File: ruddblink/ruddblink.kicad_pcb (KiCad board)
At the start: 2 copper layers, 40.6 x 48.5 mm, 30 parts, among them Q1 IRFML8244, SW1 JS202011JCQN, SW2 PTS526 SK15 SMTR2 LFS, U1 ATtiny85-20SU, U2 74HC595

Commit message: Add OSHW symbol
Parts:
- added G***: LOGO, ruddblink:OSHW-Symbol_140mil, B.Cu at (128.3, 104.1)

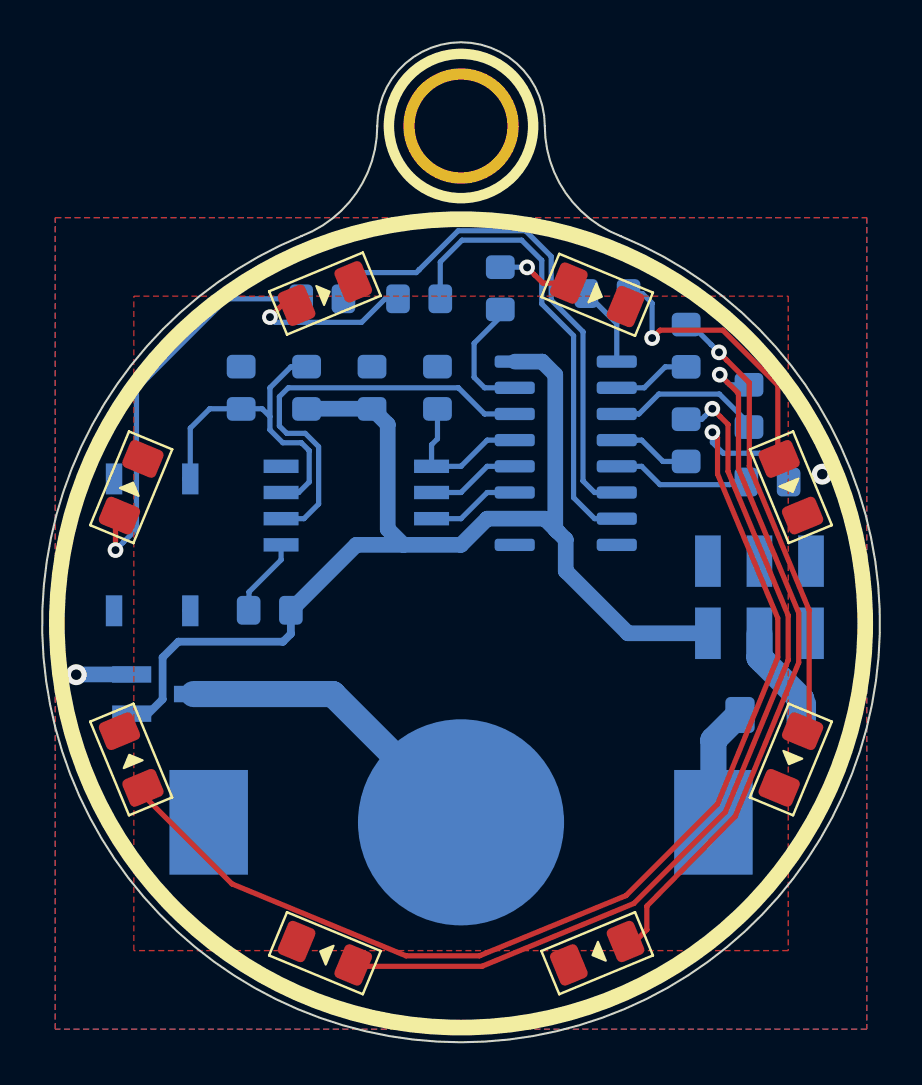
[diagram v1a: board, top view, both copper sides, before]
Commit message: Additional cosmetic edits
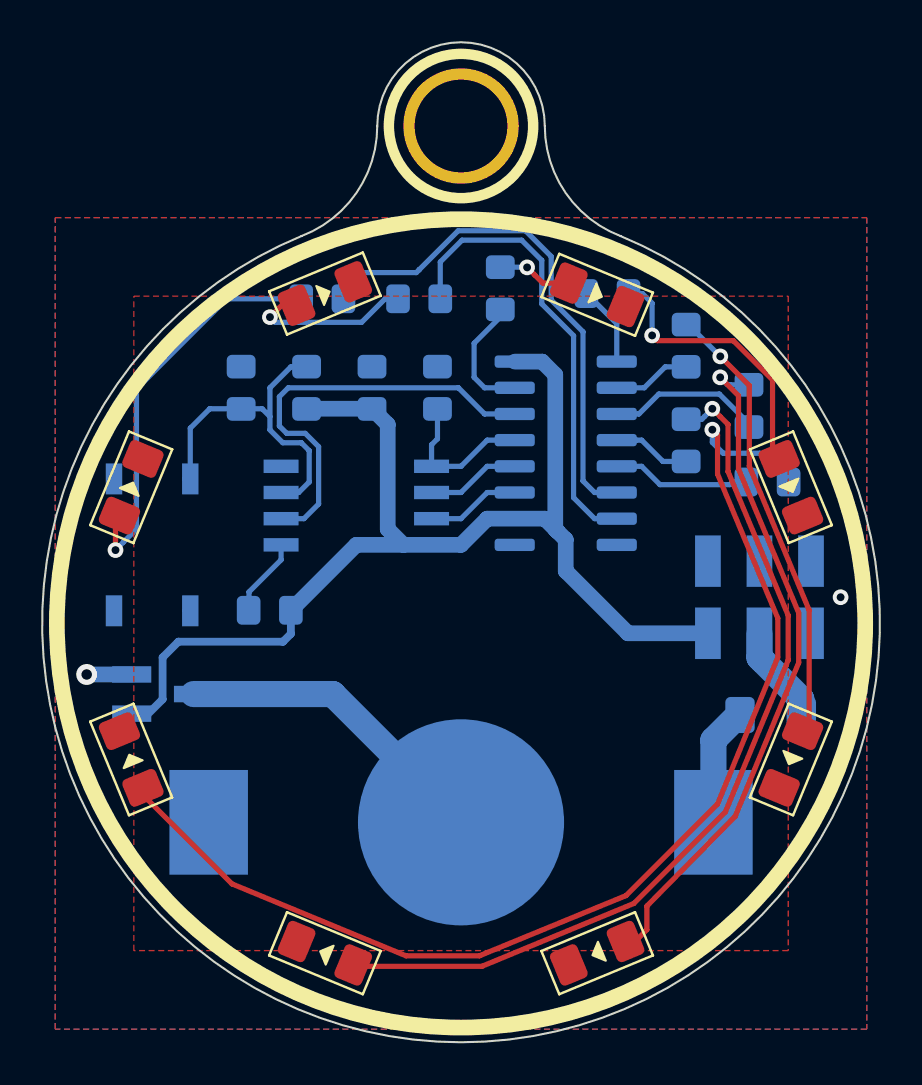
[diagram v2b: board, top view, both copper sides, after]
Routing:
- net GND: track 2.70 -> 2.18 mm
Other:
- board text added: "-"

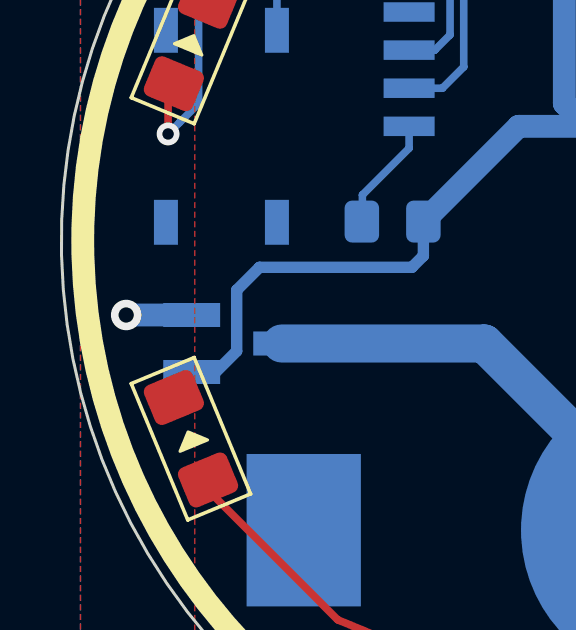
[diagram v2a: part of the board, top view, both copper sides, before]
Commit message: Fix some DFM issues
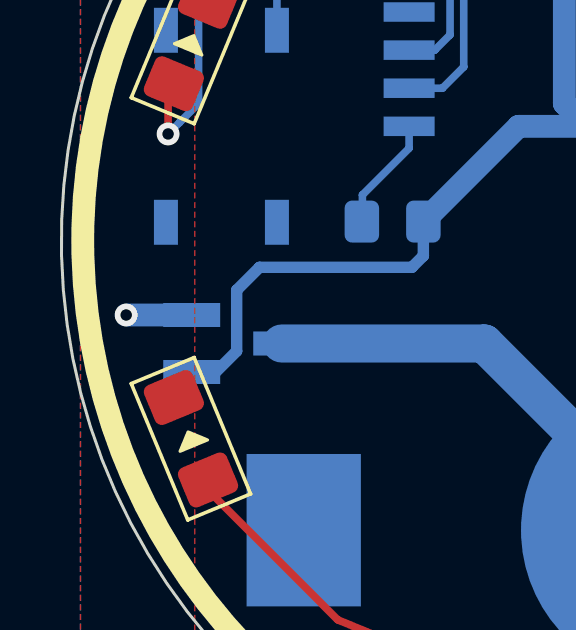
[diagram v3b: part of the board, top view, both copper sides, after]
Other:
- rule pad_to_mask_clearance: 0.0508 -> 0.0762
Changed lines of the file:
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@@
     (pad_size 10 10)
     (pad_drill 0)
-    (pad_to_mask_clearance 0.0508)
+    (pad_to_mask_clearance 0.0762)
     (solder_mask_min_width 0.1016)
     (aux_axis_origin 0 0)
@@
   )
   (gr_text JLCJLCJLCJLC (at 147.32 104.775 90) (layer B.SilkS)
-    (effects (font (size 0.8128 0.6096) (thickness 0.1016)) (justify mirror))
+    (effects (font (size 0.8128 0.6096) (thickness 0.127)) (justify mirror))
   )
   (gr_line (start 151.13 135.89) (end 133.35 92.71) (layer Dwgs.User) (width 0.1))
@@
   (via (at 160.655 113.03) (size 0.762) (drill 0.381) (layers F.Cu B.Cu) (net 1))
   (segment (start 126.262 116.779) (end 124.079 116.779) (width 0.762) (layer B.Cu) (net 1))
-  (via (at 124.079 116.779) (size 1.016) (drill 0.508) (layers F.Cu B.Cu) (net 1))
+  (via (at 124.079 116.779) (size 0.762) (drill 0.381) (layers F.Cu B.Cu) (net 1))
   (segment (start 145.436835 97.019) (end 145.445835 97.028) (width 0.254) (layer B.Cu) (net 2))
   (segment (start 144.145 97.019) (end 145.436835 97.019) (width 0.254) (layer B.Cu) (net 2))

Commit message: More cosmetic edits
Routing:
- net Net-(D8-Pad2): track 8.72 -> 9.66 mm
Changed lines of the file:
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@@
     (thickness 1.6)
     (drawings 51)
-    (tracks 211)
+    (tracks 209)
     (zones 0)
     (modules 31)
@@
     (effects (font (size 2.032 2.032) (thickness 0.508)) (justify mirror))
   )
-  (gr_text JLCJLCJLCJLC (at 147.32 104.775 90) (layer B.SilkS)
-    (effects (font (size 0.8128 0.6096) (thickness 0.127)) (justify mirror))
+  (gr_text JLCJLCJLCJLC (at 147.574 104.394 82) (layer B.SilkS)
+    (effects (font (size 0.8128 0.6096) (thickness 0.1524)) (justify mirror))
   )
   (gr_line (start 151.13 135.89) (end 133.35 92.71) (layer Dwgs.User) (width 0.1))
@@
   (segment (start 130.8735 98.552) (end 126.492 102.9335) (width 0.254) (layer B.Cu) (net 8))
   (segment (start 134.366 99.441) (end 134.366 98.933) (width 0.254) (layer F.Cu) (net 9))
-  (segment (start 133.603978 98.806) (end 133.349993 99.059985) (width 0.254) (layer F.Cu) (net 9))
-  (segment (start 134.239 98.806) (end 133.603978 98.806) (width 0.254) (layer F.Cu) (net 9))
-  (segment (start 133.349993 99.059985) (end 132.968994 99.440984) (width 0.254) (layer F.Cu) (net 9))
-  (via (at 132.968994 99.440984) (size 0.762) (drill 0.381) (layers F.Cu B.Cu) (net 9))
-  (segment (start 133.22301 99.695) (end 132.968994 99.440984) (width 0.254) (layer B.Cu) (net 9))
-  (segment (start 137.414 99.695) (end 133.22301 99.695) (width 0.254) (layer B.Cu) (net 9))
-  (segment (start 139.065 98.552) (end 138.557 98.552) (width 0.254) (layer B.Cu) (net 9))
-  (segment (start 138.557 98.552) (end 137.414 99.695) (width 0.254) (layer B.Cu) (net 9))
+  (segment (start 133.095945 99.821945) (end 132.842 99.568) (width 0.254) (layer B.Cu) (net 9))
+  (segment (start 139.065 98.552) (end 137.795055 99.821945) (width 0.254) (layer B.Cu) (net 9))
+  (segment (start 137.795055 99.821945) (end 133.095945 99.821945) (width 0.254) (layer B.Cu) (net 9))
+  (via (at 132.842 99.568) (size 0.762) (drill 0.381) (layers F.Cu B.Cu) (net 9))
+  (segment (start 134.62 98.806) (end 132.842 99.568) (width 0.254) (layer F.Cu) (net 9))
+  (segment (start 134.261729 98.867242) (end 134.62 98.806) (width 0.254) (layer F.Cu) (net 9))
   (segment (start 158.75 117.983) (end 158.75 118.745) (width 1.27) (layer B.Cu) (net 10))
   (segment (start 156.845 116.078) (end 158.75 117.983) (width 1.27) (layer B.Cu) (net 10))
